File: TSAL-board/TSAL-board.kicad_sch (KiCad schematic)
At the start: 0 parts

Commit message: 素子追加
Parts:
- added J1: 19427-0040, ProjectEV:Connector_MX150L_19427-0040, symbol ProjectEV:Connector_MX150L_19427-0040
- added R1, R2, R3, R4, R5, R6, R7, R8: 1M, Resistor_SMD:R_2010_5025Metric, symbol ProjectEV:R
- added U1: TL431QDBVR, ProjectEV:Package_SOT-23-5_TL431QDBVR, symbol ProjectEV:Reference_TL431QDBVR

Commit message: 素子追加
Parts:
- added R10: 10k, Resistor_SMD:R_0603_1608Metric, symbol ProjectEV:R
- added R9: 19.1k, Resistor_SMD:R_0603_1608Metric, symbol ProjectEV:R
- added U2: TLP291(GB,SE, ProjectEV:Isolator_TLP291(GB,SE, symbol ProjectEV:Isolator_TLP291(GB,SE
- R1, R2, R3, R4, R5, R6, R7, R8: value 1M -> 220k; footprint Resistor_SMD:R_2010_5025Metric -> ProjectEV:R_VishayDale_RCC1206-e3; Package 5025 -> 3216
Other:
- note added: "ERJ-3EKF1912V"
- note added: "RCC1206220KFKEA x 8"
- moved on the sheet: U1

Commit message: 回路図完成
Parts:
- added C1, C8: 0.1u, Capacitor_SMD:C_0603_1608Metric, symbol ProjectEV:C
- added C10: 1000p, Capacitor_SMD:C_1206_3216Metric, symbol ProjectEV:C
- added C2, C3, C4, C5: 10u, Capacitor_SMD:C_1206_3216Metric, symbol ProjectEV:C
- added C6, C7: 1u, Capacitor_SMD:C_0805_2012Metric, symbol ProjectEV:C
- added C9: 10n, Capacitor_SMD:C_0603_1608Metric, symbol ProjectEV:C
- added D1: PZ1AH11B-AU, ProjectEV:D_SOD-123HE_PZ1AHxxxB-AU, symbol ProjectEV:D_PZ1AH11B-AU
- added D2, D3: DFLZ24Q-7, ProjectEV:D_PowerDI-123_DFLZxxQ, symbol ProjectEV:D_DFLZ24Q-7
- added D4: LED, LED_SMD:LED_0603_1608Metric, symbol Device:LED
- added F1: 0ABB-1000-TM, ProjectEV:Fuse_0ABB, symbol ProjectEV:Fuse_0ABB-1000-TM
- added H1, H2, H3, H4: M3, MountingHole:MountingHole_3.2mm_M3_Pad_Via, symbol Mechanical:MountingHole_Pad
- added J1, J3, J4: BM02B-PASS-1-TF, ProjectEV:Connector_BM02B-PASS-1-TF, symbol ProjectEV:Connector_BM02B-PASS-1-TF
- added Q1: DMP3098LQ-7, ProjectEV:Package_SOT-23_DMP3098LQ-7, symbol ProjectEV:Transistor_DMP3098LQ-7
- added Q2, Q3, Q4: 2N7002K-AU, ProjectEV:Package_SOT-23_2N7002K-AU, symbol ProjectEV:Transistor_2N7002K-AU
- added R1, R28: 100k, Resistor_SMD:R_0603_1608Metric, symbol ProjectEV:R
- added R11: 3.9k, Resistor_SMD:R_0603_1608Metric, symbol ProjectEV:R
- added R12, R13, R14, R15, R16, R17, R18, R19, R20, R21: 15k, ProjectEV:R_TEConnectivity_3502, symbol ProjectEV:R
- added R23, R25: 10k, Resistor_SMD:R_0603_1608Metric, symbol ProjectEV:R
- added R24, R32: 1M, Resistor_SMD:R_0603_1608Metric, symbol ProjectEV:R
- added R26: 180k, Resistor_SMD:R_0603_1608Metric, symbol ProjectEV:R
- added R27, R30, R31: 100, Resistor_SMD:R_0603_1608Metric, symbol ProjectEV:R
- added R29: 1M, Resistor_SMD:R_1206_3216Metric, symbol ProjectEV:R
- added R33, R34: 0, Resistor_SMD:R_0603_1608Metric, symbol ProjectEV:R
- added U3: TLC555QDRQ1, ProjectEV:Package_SOIC-8_3.9x4.9mm_P1.27mm_TLC555QDRQ1, symbol ProjectEV:Timer_TLC555QDRQ1
- R10: renamed from R9; value 19.1k -> 15.4k
- renumbered J1 to J2, R1 to R2, R10 to R22, R2 to R3, R3 to R4, R4 to R5, R5 to R6, R6 to R7, R7 to R8, R8 to R9
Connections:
- net at R4.1: now also R3.2
- net at R4.2: now also R5.1
- net TS+: now reaches R2.1
- net TS+: now also J2.1 (Pin_1), R6.1, R12.1, R17.1
- net at R2.2: now also R3.1
- net at R22.1: now also U2.1 (Anode), D2.1 (K), R16.2, R21.2
- net at R22.2: now also U1.3 (K), U2.2 (Cathode)
- net at R5.2: now also R10.1, R9.2, U1.4 (REF), D3.1 (K)
- net at R6.2: now also R7.1
- net at R10.2: now also R11.1
- net at R8.1: now also R7.2
- net at R8.2: now also R9.1
- net TS-: now reaches U1.5 (A)
- net TS-: now also J2.2 (Pin_2), D2.2 (A), D3.2 (A), R11.2
- net GND: now reaches U2.3 (Emitter)
- net GND: now also C1.2, C10.2, C3.2, C5.2, C6.2, C7.1, C8.1, C9.1, D4.1 (K), J1.2 (Pin_2), J1.MP1 (MountPin), J1.MP2 (MountPin), J3.MP1 (MountPin), J3.MP2 (MountPin), J4.MP1 (MountPin), J4.MP2 (MountPin), Q2.2 (S), Q3.2 (S), Q4.2 (S), R1.2, R29.2, R32.2, U3.1 (GND)
- net ~{TS_ACTIVE}: now reaches U2.4 (Collector)
- net ~{TS_ACTIVE}: now also R24.2, R27.1, R31.1
- new net: C10.1, H1.1, R29.1
- new net: D1.2 (A), Q1.1 (G), R1.1
- new net: F1.2, Q1.3 (D)
- new net: J3.1 (Pin_1), R33.2
- new net: J3.2 (Pin_2), Q3.3 (D)
- new net: R19.2, R20.1
- new net: R20.2, R21.1
- new net: R14.2, R15.1
- new net: R15.2, R16.1
- new net: C6.1, R26.2, U3.2 (TRIG), U3.6 (THRES)
- new net: C9.2, U3.5 (CONT)
- new net: R25.2, R26.1, U3.7 (DISCH)
- new net: C2.2, C3.1
- new net: Q3.1 (G), R31.2
- new net: J4.1 (Pin_1), R34.2
- new net: J4.2 (Pin_2), Q4.3 (D)
- new net: Q2.1 (G), R27.2
- new net: Q4.1 (G), R30.2, R32.1
- new net: R12.2, R13.1
- new net: R13.2, R14.1
- new net: C4.2, C5.1
- new net: D4.2 (A), R23.2
- new net: R17.2, R18.1
- new net: R18.2, R19.1
- new net +12V: C1.1, C2.1, C4.1, C7.2, C8.2, D1.1 (K), Q1.2 (S), R23.1, R24.1, R25.1, R28.1, R33.1, R34.1, U3.8 (VDD)
- new net GLV_IN: F1.1, J1.1 (Pin_1)
- new net RED_SIG: R30.1, U3.3 (OUT)
- new net ~{RST}: Q2.3 (D), R28.2, U3.4 (~{RESET})
- no-connect marks 0 -> 3
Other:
- note added: "15kOhms x10 (5025, 2W) Max 5.3mA ,0.42W (V_{TS+} - V_{TS-} = 400V) 安全係数0.25 (2W x 0.25 = 0.5W > 0.42W)"
- note added: "32VDC, 1A"
- note added: "350215KJT x 10"
- note added: "DC BIAS Cap. Change Rate -11.1% (12V)"
- note added: "GCM21BR71H105KA03L"
- note added: "HIGH VOLTAGE"
- note added: "V_{th} = 2.495 x {(440k + R10 + R11) / (R10 + R11)} V_{th} = 60.3V sim結果 V_{th} = 60.5V"
- note added: "Vz = 24V"
- note added: "f = 1.44/{(R25 + 2 x R26) x C1} f = 3.89Hz Cap. Tolerance +-10% f_{Max} = 4.93Hz (including DC Bias:-11.1%) f_{Min} = 3.54Hz"
- note removed: "ERJ-3EKF1912V"
- moved on the sheet: J2, R10, R2, R22, R3, R4, R5, R6, R7, R8, R9, U1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

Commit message: コメント追加
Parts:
- added R35: 100k, Resistor_SMD:R_0603_1608Metric, symbol ProjectEV:R
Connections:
- net +12V: now also R35.1
- net RED_SIG: now also R35.2
- net TSAL_GREEN_A: now reaches J3.1 (Pin_1), R33.2
- net TSAL_RED_A: now reaches J4.1 (Pin_1), R34.2
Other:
- note added: "100V"
- note added: "1kV"
- note added: "220kOhms x 8 (3216, 0.5W) Max 450uA, 0.045W 安全係数0.25 (0.5W x 0.25 = 0.125 > 0.045W)"
- note added: "350215KJT x 10 Operating Voltage 200V"
- note added: "80V"
- note added: "RCC1206220KFKEA x 8 Operating Voltage 200V"
- note added: "V_{th} = 2.495 x {(440k + R10 + R11) / (R10 + R11)} V_{th} = 59.4V sim結果 V_{th} = 59.6V"
- note removed: "350215KJT x 10"
- note removed: "RCC1206220KFKEA x 8"
- note removed: "V_{th} = 2.495 x {(440k + R10 + R11) / (R10 + R11)} V_{th} = 60.3V sim結果 V_{th} = 60.5V"
- moved on the sheet: R33, R34

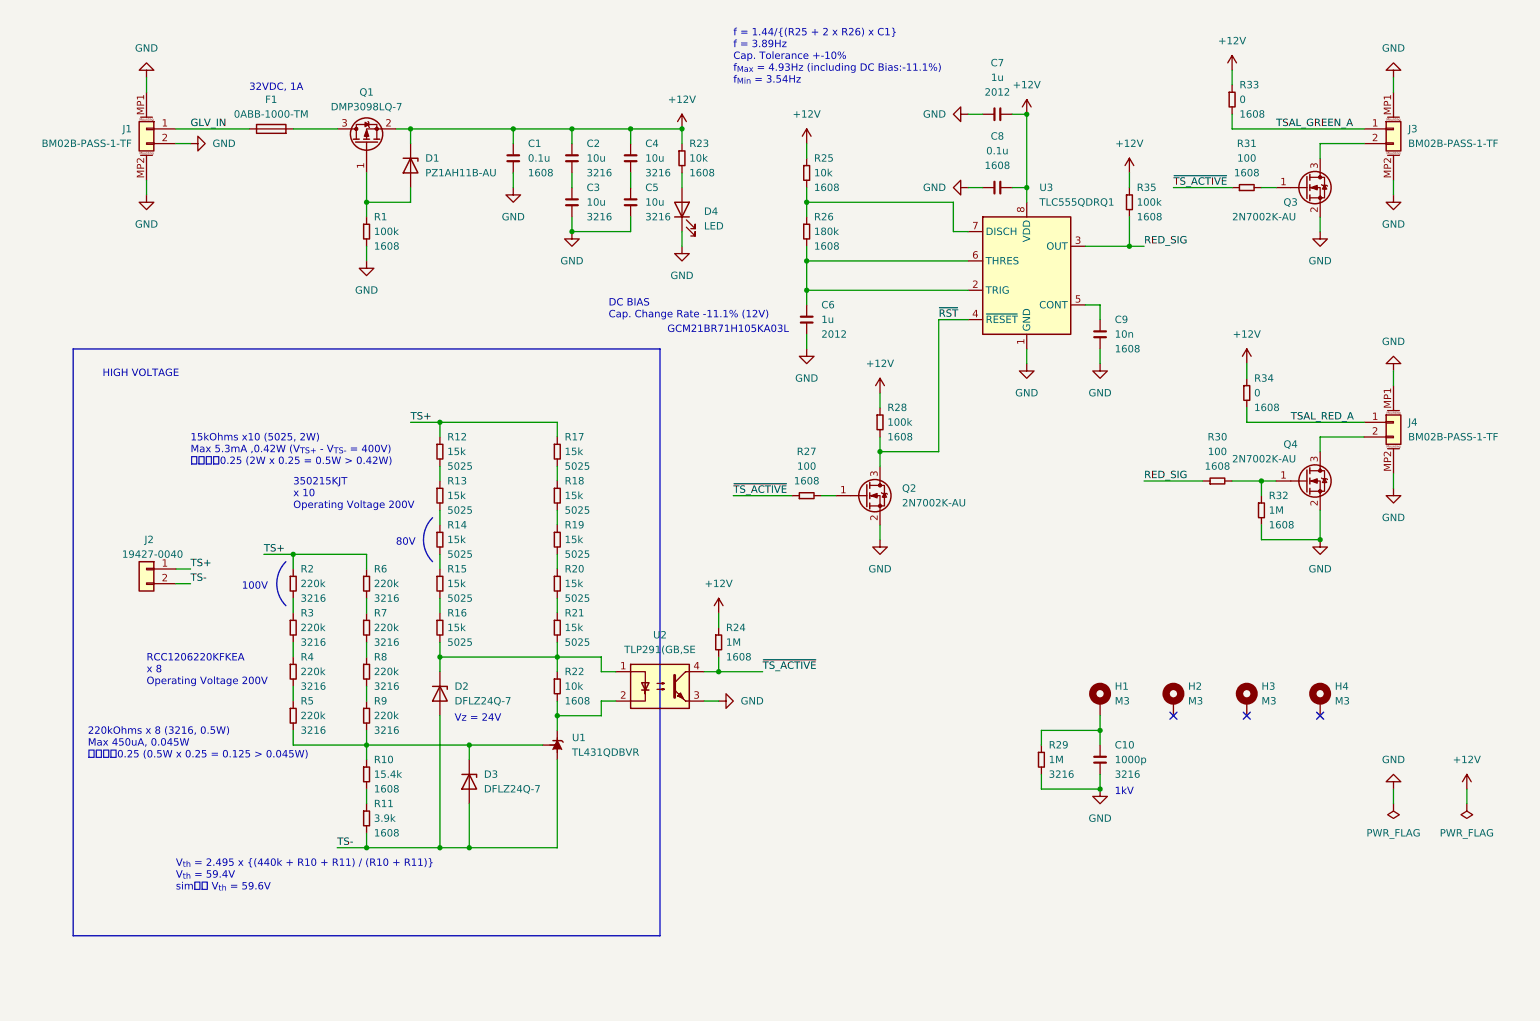
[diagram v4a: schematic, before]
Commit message: 補償回路、シュミットトリガ回路追加
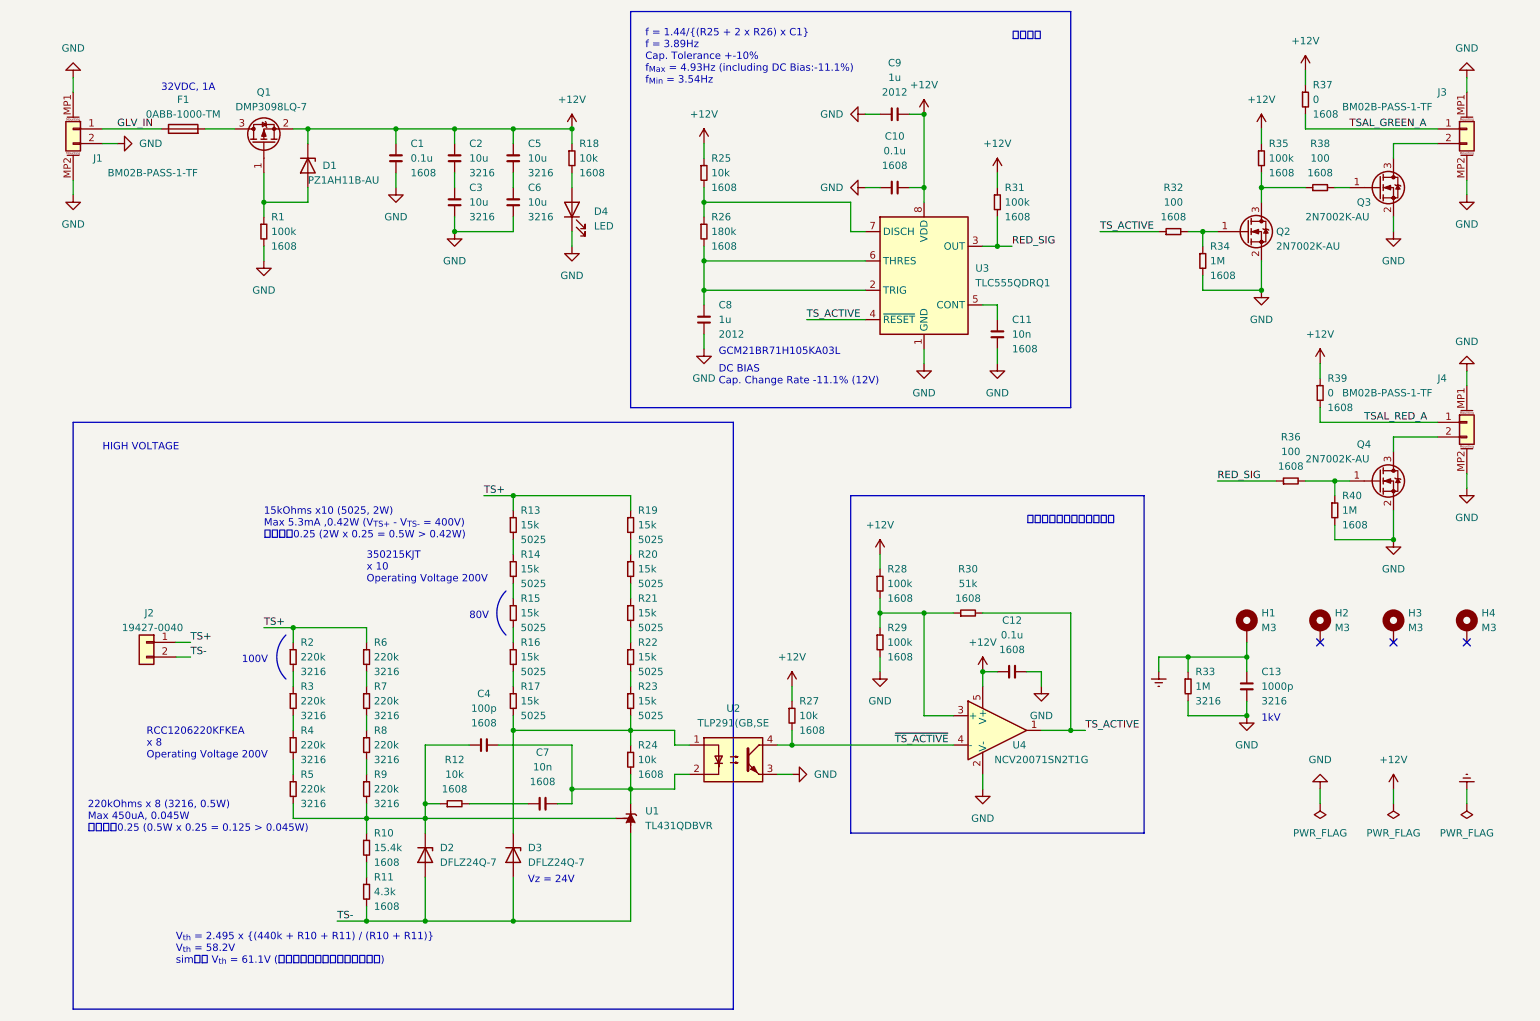
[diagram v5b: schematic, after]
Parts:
- removed R27: 100, Resistor_SMD:R_0603_1608Metric, symbol ProjectEV:R
- added C12: 0.1u, Capacitor_SMD:C_0603_1608Metric, symbol ProjectEV:C
- added C4: 100p, Capacitor_SMD:C_0603_1608Metric, symbol ProjectEV:C
- added C7: 10n, Capacitor_SMD:C_0603_1608Metric, symbol ProjectEV:C
- added R12: 10k, Resistor_SMD:R_0603_1608Metric, symbol ProjectEV:R
- added R29, R35: 100k, Resistor_SMD:R_0603_1608Metric, symbol ProjectEV:R
- added R30: 51k, Resistor_SMD:R_0603_1608Metric, symbol ProjectEV:R
- added R32: 100, Resistor_SMD:R_0603_1608Metric, symbol ProjectEV:R
- added R34: 1M, Resistor_SMD:R_0603_1608Metric, symbol ProjectEV:R
- added U4: NCV20071SN2T1G, ProjectEV:Package_SOT-23-5_NCV20071SN2T1G, symbol ProjectEV:Opamp_NCV20071SN2T1G
- R11: value 3.9k -> 4.3k
- R27: renamed from R24; value 1M -> 10k
- renumbered C8 to C10, C9 to C11, C10 to C13, C4 to C5, C5 to C6, C6 to C8, C7 to C9, D3 to D2, D2 to D3, R12 to R13, R13 to R14, R14 to R15, R15 to R16, R16 to R17, R23 to R18, R17 to R19, R18 to R20, R19 to R21, R20 to R22, R21 to R23, R22 to R24, R35 to R31, R29 to R33, R30 to R36, R33 to R37, R31 to R38, R34 to R39, R32 to R40
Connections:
- net +12V: now also C12.2, R35.1, U4.5 (V+)
- net GND: now also C12.1, R29.2, R34.2, U4.2 (V-)
- net ~{TS_ACTIVE}: now also U4.4 (-); no longer R38.1
- net Earth: now reaches C13.1, H1.1, R33.1
- net at R24.2, U1.3 (K), U2.2 (Cathode): now also C4.1, C7.1
- net at D2.1 (K), R10.1, R5.2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: now also C4.2, R12.1
- net at Q2.1 (G): now also R32.2, R34.1
- removed net ~{RST}: Q2.3 (D), R28.2, U3.4 (~{RESET})
- new net: R28.2, R29.1, R30.1, U4.3 (+)
- new net: C7.2, R12.2
- new net: Q2.3 (D), R35.2, R38.1
- new net TS_ACTIVE: R30.2, R32.1, U3.4 (~{RESET}), U4.1
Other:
- note added: "V_{th} = 2.495 x {(440k + R10 + R11) / (R10 + R11)} V_{th} = 58.2V sim結果 V_{th} = 61.1V (遅れ補償分計算値からズレあり)"
- note added: "シュミットトリガ（反転）"
- note added: "点滅回路"
- note removed: "V_{th} = 2.495 x {(440k + R10 + R11) / (R10 + R11)} V_{th} = 59.4V sim結果 V_{th} = 59.6V"
- moved on the sheet: C1, C10, C11, C13, C2, C3, C5, C6, C8, C9, D1, D2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

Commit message: sim結果追記
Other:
- note added: "V_{th} = 2.495 x {(440k + R10 + R11) / (R10 + R11)} V_{th} = 58.2V sim結果 V_{th} = L -> H : 63.2V, H -> L : 47.8V (遅れ補償、シュミットトリガ分計算値からズレあり)"
- note removed: "V_{th} = 2.495 x {(440k + R10 + R11) / (R10 + R11)} V_{th} = 58.2V sim結果 V_{th} = 61.1V (遅れ補償分計算値からズレあり)"

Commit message: 閾値設定用の抵抗修正
回路図のみ、PCBやガーバーなどその他ファイルには未反映
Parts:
- R10: value 15.4k -> 17.8k
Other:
- note added: "V_{th} = 2.495 x {(440k + R10 + R11) / (R10 + R11)} V_{th} = 52.2V sim結果 V_{th} = L -> H : 59.8V, H -> L : 42.1V (遅れ補償、シュミットトリガ分計算値からズレあり)"
- note removed: "V_{th} = 2.495 x {(440k + R10 + R11) / (R10 + R11)} V_{th} = 58.2V sim結果 V_{th} = L -> H : 63.2V, H -> L : 47.8V (遅れ補償、シュミットトリガ分計算値からズレあり)"
